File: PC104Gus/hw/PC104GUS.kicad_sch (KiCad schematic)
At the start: 40 parts, among them J1 IRQDMA_JP, J2 Conn_02x31_Top_Bottom, J3 Bus_ISA_8bit, J4 Conn_01x04_Pin, J5 SJ1-3535NG, J6 UART_TX, J7 Conn_01x02_Pin, J8 SJ1-3535NG, U1 Pico, U10 74LVC2G06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

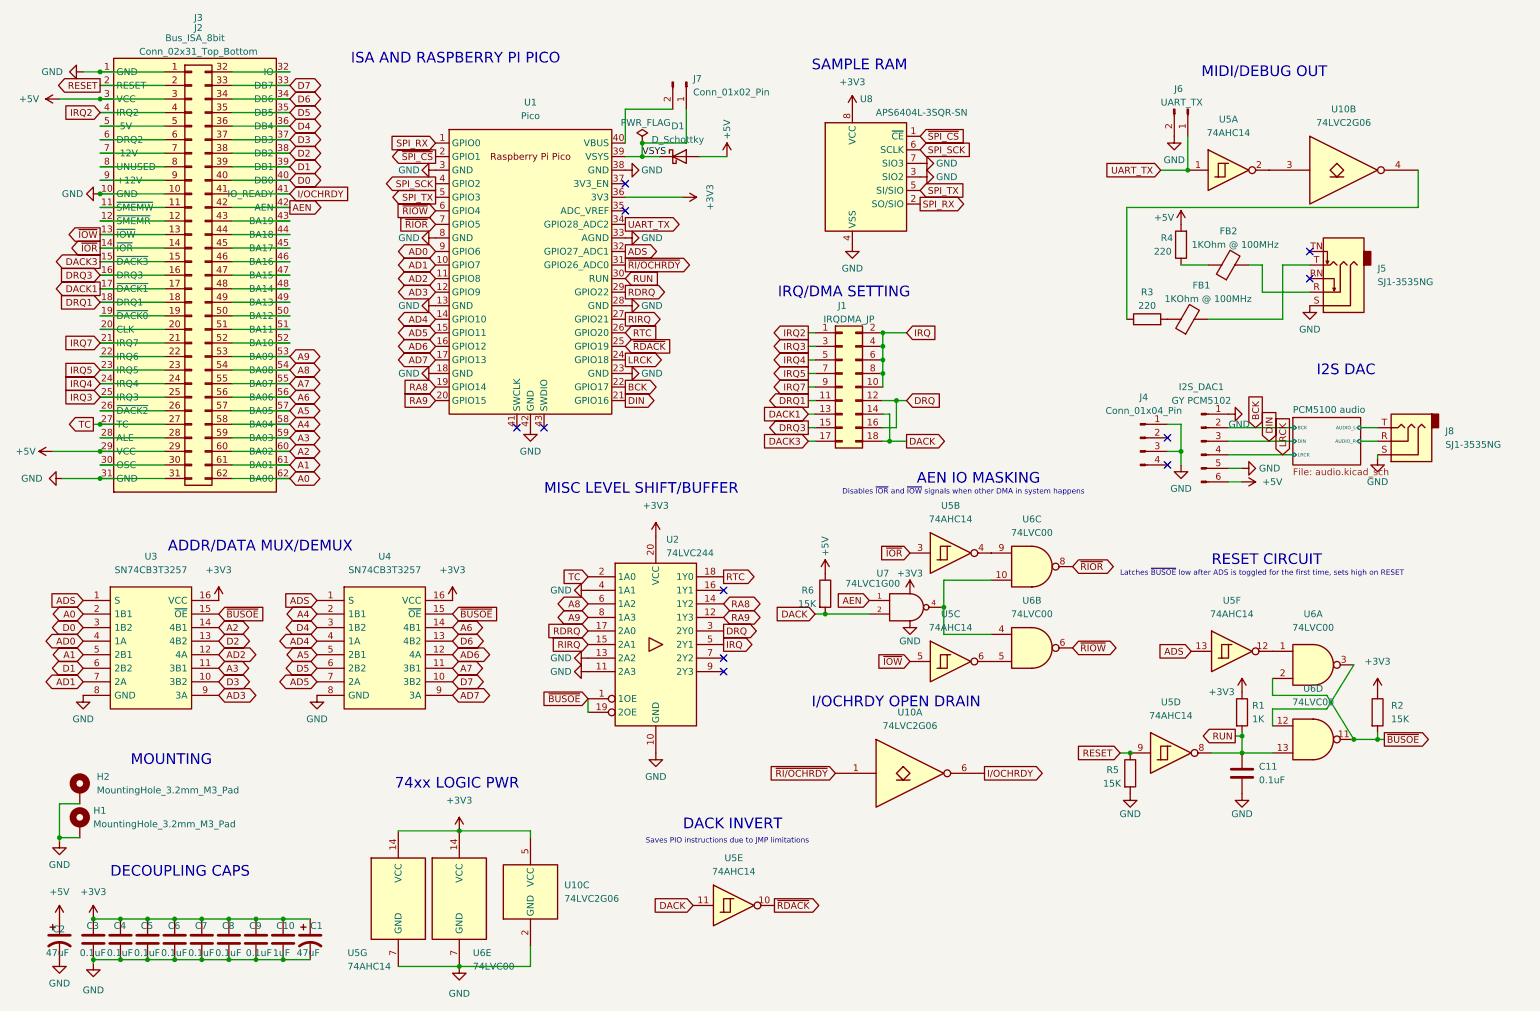
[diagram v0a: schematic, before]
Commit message: Part position complete
Added all parts, sorted part numbering and foot prints.
Beginning routing
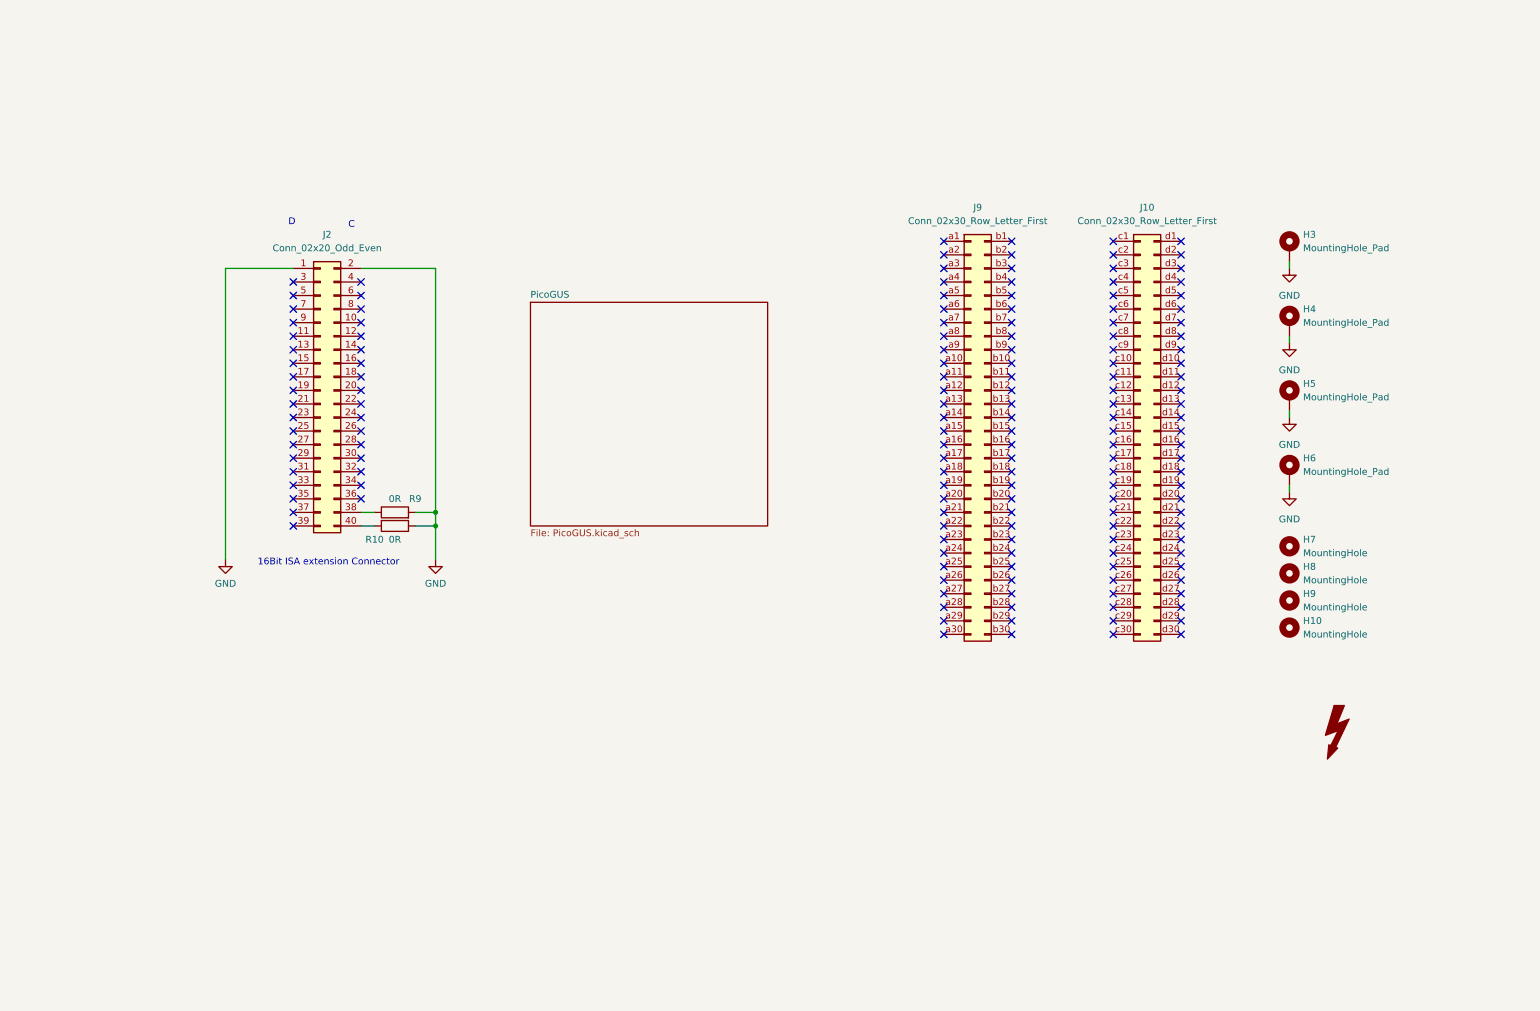
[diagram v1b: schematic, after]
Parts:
- removed C1, C2: 47uF, Capacitor_SMD:C_1206_3216Metric, symbol Device:C_Polarized_US
- removed C10: 1uF, Capacitor_SMD:C_0805_2012Metric, symbol Device:C
- removed C11, C3, C4, C5, C6, C7, C8, C9: 0.1uF, Capacitor_SMD:C_0805_2012Metric, symbol Device:C
- removed D1: D_Schottky, Diode_SMD:D_SOD-123, symbol Device:D_Schottky
- removed FB1, FB2: 1KOhm @ 100MHz, Inductor_SMD:L_0805_2012Metric, symbol Device:FerriteBead
- removed H1, H2: MountingHole_3.2mm_M3_Pad, MountingHole:MountingHole_3.2mm_M3_Pad, symbol Mechanical:MountingHole_Pad
- removed I2S_DAC1: GY PCM5102, Connector_PinHeader_2.54mm:PinHeader_1x06_P2.54mm_Vertical, symbol Connector:Conn_01x06_Pin
- removed J1: IRQDMA_JP, Connector_PinHeader_2.54mm:PinHeader_2x09_P2.54mm_Vertical, symbol Connector_Generic:Conn_02x09_Odd_Even
- removed J2: Conn_02x31_Top_Bottom, Connector_PinHeader_2.54mm:PinHeader_2x31_P2.54mm_Vertical, symbol Connector_Generic:Conn_02x31_Top_Bottom
- removed J3: Bus_ISA_8bit, PiGUS library:BUS_PC_chamfer, symbol Connector:Bus_ISA_8bit
- removed J4: Conn_01x04_Pin, Connector_PinHeader_2.54mm:PinHeader_1x04_P2.54mm_Vertical, symbol Connector:Conn_01x04_Pin
- removed J5: SJ1-3535NG, Connector_Audio:Jack_3.5mm_CUI_SJ1-3535NG_Horizontal, symbol Connector:AudioJack3_SwitchTR
- removed J6: UART_TX, Connector_PinHeader_2.54mm:PinHeader_1x02_P2.54mm_Vertical, symbol Connector:Conn_01x02_Male
- removed J7: Conn_01x02_Pin, Connector_PinHeader_2.54mm:PinHeader_1x02_P2.54mm_Vertical, symbol Connector:Conn_01x02_Pin
- removed J8: SJ1-3535NG, Connector_Audio:Jack_3.5mm_CUI_SJ1-3535NG_Horizontal, symbol Connector_Audio:AudioJack3
- removed R1: 1K, Resistor_SMD:R_0805_2012Metric, symbol Device:R
- removed R2, R5, R6: 15K, Resistor_SMD:R_0805_2012Metric, symbol Device:R
- removed R3, R4: 220, Resistor_SMD:R_0805_2012Metric, symbol Device:R
- removed U1: Pico, PiGUS library:RPi_Pico_SMD_TH, symbol PiGUS library:Pico
- removed U10: 74LVC2G06, Package_SO:TSOP-6_1.65x3.05mm_P0.95mm, symbol 74xGxx:74LVC2G06
- removed U2: 74LVC244, Package_SO:TSSOP-20_4.4x6.5mm_P0.65mm, symbol 74xx:74HC244
- removed U3, U4: SN74CB3T3257, Package_SO:TSSOP-16_4.4x5mm_P0.65mm, symbol PiGUS library:74FST3257DR2G
- removed U5: 74AHC14, Package_SO:SOIC-14_3.9x8.7mm_P1.27mm, symbol 74xx:74LS14
- removed U6: 74LVC00, Package_SO:SOIC-14_3.9x8.7mm_P1.27mm, symbol 74xx:74LS00
- removed U7: 74LVC1G00, Package_TO_SOT_SMD:SOT-23-5, symbol 74xGxx:74LVC1G00
- removed U8: APS6404L-3SQR-SN, Package_SO:SOIC-8_3.9x4.9mm_P1.27mm, symbol Memory_RAM:ESP-PSRAM32
- added FOX1: SYM_Flash_Large, PaulasKiCADFootPrint:Fox_avatar_18mm, symbol Graphic:SYM_Flash_Large
- added H10, H7, H8, H9: MountingHole, MountingHole:MountingHole_2mm, symbol Mechanical:MountingHole
- added H3, H4, H5, H6: MountingHole_Pad, MountingHole:MountingHole_3.2mm_M3_Pad_TopBottom, symbol Mechanical:MountingHole_Pad
- added J10, J9: Conn_02x30_Row_Letter_First, Connector_PinSocket_2.00mm:PinSocket_2x30_P2.00mm_Vertical, symbol Connector_Generic:Conn_02x30_Row_Letter_First
- added J2: Conn_02x20_Odd_Even, Connector_PinSocket_2.54mm:PinSocket_2x20_P2.54mm_Vertical, symbol Connector_Generic:Conn_02x20_Odd_Even
- added R10, R9: 0R, Resistor_SMD:R_0603_1608Metric, symbol Device:R
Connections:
- net GND: now also H3.1, H4.1, H5.1, H6.1, J2.1 (Pin_1), J2.2 (Pin_2), R10.1, R9.2
- new net: J2.38 (Pin_38), R9.1
- new net: J2.40 (Pin_40), R10.2
- no-connect marks 11 -> 156
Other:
- removed sheet PCM5100 audio
- added sheet PicoGUS (PicoGUS.kicad_sch)
- note added: "16Bit ISA extension Connector"
- note added: "C"
- note added: "D"
- note removed: "74xx LOGIC PWR"
- note removed: "ADDR/DATA MUX/DEMUX"
- note removed: "AEN IO MASKING"
- note removed: "DACK INVERT"
- note removed: "DECOUPLING CAPS"
- note removed: "Disables ~{IOR} and ~{IOW} signals when other DMA in system happens"
- note removed: "I/OCHRDY OPEN DRAIN"
- note removed: "I2S DAC"
- note removed: "IRQ/DMA SETTING"
- note removed: "ISA AND RASPBERRY PI PICO"
- note removed: "Latches ~{BUSOE} low after ADS is toggled for the first time, sets high on RESET"
- note removed: "MIDI/DEBUG OUT"
- note removed: "MISC LEVEL SHIFT/BUFFER"
- note removed: "MOUNTING"
- note removed: "RESET CIRCUIT"
- note removed: "SAMPLE RAM"
- note removed: "Saves PIO instructions due to JMP limitations"
- title: PicoGUS -> (none)

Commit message: PC104GUS production files
Production files generated. This build worked!
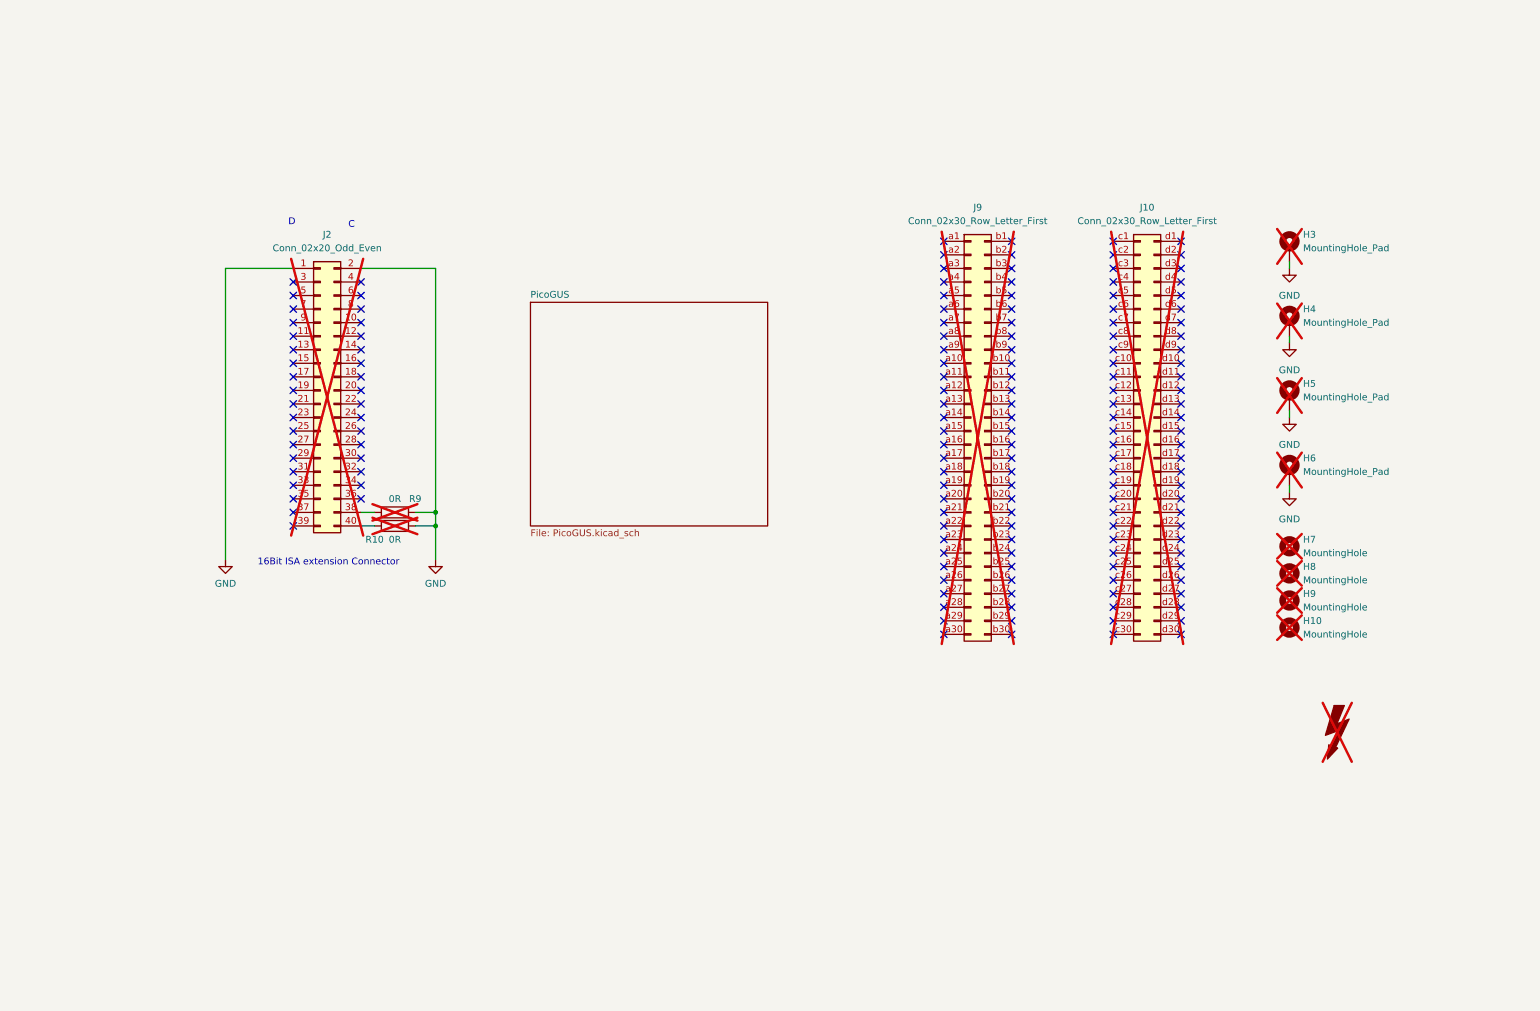
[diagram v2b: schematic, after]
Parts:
- FOX1, J10, J2, J9, R10, R9: LCSC (none) -> DNF; now not fitted
- H10, H3, H4, H5, H6, H7, H8, H9: LCSC (none) -> DNF; now not fitted; now in the parts list
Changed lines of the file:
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@@
 		(unit 1)
 		(exclude_from_sim yes)
-		(in_bom no)
-		(on_board yes)
-		(dnp no)
+		(in_bom yes)
+		(on_board yes)
+		(dnp yes)
 		(fields_autoplaced yes)
 		(property "Reference" "H9"
@@
 			)
 		)
+		(property "LCSC" "DNF"
+			(at 251.46 123.19 0)
+			(effects
+				(font
+					(size 1.27 1.27)
+				)
+				(hide yes)
+			)
+		)
 		(instances
 			(project "PC104GUS"
@@
 		(in_bom yes)
 		(on_board yes)
-		(dnp no)
+		(dnp yes)
 		(fields_autoplaced yes)
 		(property "Reference" "J9"
@@
 			)
 		)
+		(property "LCSC" "DNF"
+			(at 191.77 91.44 0)
+			(effects
+				(font
+					(size 1.27 1.27)
+				)
+				(hide yes)
+			)
+		)
 		(pin "b29"
 		)
@@
 		(unit 1)
 		(exclude_from_sim yes)
-		(in_bom no)
-		(on_board yes)
-		(dnp no)
+		(in_bom yes)
+		(on_board yes)
+		(dnp yes)
 		(fields_autoplaced yes)
 		(property "Reference" "H3"
@@
 			)
 		)
+		(property "LCSC" "DNF"
+			(at 251.46 57.15 0)
+			(effects
+				(font
+					(size 1.27 1.27)
+				)
+				(hide yes)
+			)
+		)
 		(pin "1"
 		)
@@
 		(at 260.35 147.32 0)
 		(unit 1)
-		(exclude_from_sim no)
-		(in_bom yes)
-		(on_board yes)
-		(dnp no)
+		(exclude_from_sim yes)
+		(in_bom yes)
+		(on_board yes)
+		(dnp yes)
 		(fields_autoplaced yes)
 		(property "Reference" "FOX1"
@@
 			)
 		)
-		(property "Sim.Enable" "0"
-			(at 260.35 147.32 0)
+		(property "LCSC" "DNF"
+			(at 260.35 147.32 90)
 			(effects
 				(font
@@
 		(unit 1)
 		(exclude_from_sim yes)
-		(in_bom no)
-		(on_board yes)
-		(dnp no)
+		(in_bom yes)
+		(on_board yes)
+		(dnp yes)
 		(fields_autoplaced yes)
 		(property "Reference" "H7"
@@
 		)
 		(property "Description" "Mounting Hole without connection"
+			(at 251.46 113.03 0)
+			(effects
+				(font
+					(size 1.27 1.27)
+				)
+				(hide yes)
+			)
+		)
+		(property "LCSC" "DNF"
 			(at 251.46 113.03 0)
 			(effects
@@
 		(in_bom yes)
 		(on_board yes)
-		(dnp no)
+		(dnp yes)
 		(property "Reference" "R9"
 			(at 87.63 104.14 90)
@@
 			)
 		)
+		(property "LCSC" "DNF"
+			(at 83.82 106.68 90)
+			(effects
+				(font
+					(size 1.27 1.27)
+				)
+				(hide yes)
+			)
+		)
 		(pin "2"
 		)
@@
 		(unit 1)
 		(exclude_from_sim yes)
-		(in_bom no)
-		(on_board yes)
-		(dnp no)
+		(in_bom yes)
+		(on_board yes)
+		(dnp yes)
 		(fields_autoplaced yes)
 		(property "Reference" "H4"
@@
 		)
 		(property "Description" "Mounting Hole with connection"
+			(at 251.46 71.12 0)
+			(effects
+				(font
+					(size 1.27 1.27)
+				)
+				(hide yes)
+			)
+		)
+		(property "LCSC" "DNF"
 			(at 251.46 71.12 0)
 			(effects
@@
 		(in_bom yes)
 		(on_board yes)
-		(dnp no)
+		(dnp yes)
 		(property "Reference" "R10"
 			(at 80.01 111.76 90)
@@
 			)
 		)
+		(property "LCSC" "DNF"
+			(at 83.82 109.22 90)
+			(effects
+				(font
+					(size 1.27 1.27)
+				)
+				(hide yes)
+			)
+		)
 		(pin "2"
 		)
@@
 		(unit 1)
 		(exclude_from_sim yes)
-		(in_bom no)
-		(on_board yes)
-		(dnp no)
+		(in_bom yes)
+		(on_board yes)
+		(dnp yes)
 		(fields_autoplaced yes)
 		(property "Reference" "H6"
@@
 		)
 		(property "Description" "Mounting Hole with connection"
+			(at 251.46 99.06 0)
+			(effects
+				(font
+					(size 1.27 1.27)
+				)
+				(hide yes)
+			)
+		)
+		(property "LCSC" "DNF"
 			(at 251.46 99.06 0)
 			(effects
@@
 		(unit 1)
 		(exclude_from_sim yes)
-		(in_bom no)
-		(on_board yes)
-		(dnp no)
+		(in_bom yes)
+		(on_board yes)
+		(dnp yes)
 		(fields_autoplaced yes)
 		(property "Reference" "H5"
@@
 			)
 		)
+		(property "LCSC" "DNF"
+			(at 251.46 85.09 0)
+			(effects
+				(font
+					(size 1.27 1.27)
+				)
+				(hide yes)
+			)
+		)
 		(pin "1"
 		)
@@
 		(unit 1)
 		(exclude_from_sim yes)
-		(in_bom no)
-		(on_board yes)
-		(dnp no)
+		(in_bom yes)
+		(on_board yes)
+		(dnp yes)
 		(fields_autoplaced yes)
 		(property "Reference" "H10"
@@
 			)
 		)
+		(property "LCSC" "DNF"
+			(at 251.46 128.27 0)
+			(effects
+				(font
+					(size 1.27 1.27)
+				)
+				(hide yes)
+			)
+		)
 		(instances
 			(project "PC104GUS"
@@
 		(in_bom yes)
 		(on_board yes)
-		(dnp no)
+		(dnp yes)
 		(fields_autoplaced yes)
 		(property "Reference" "J10"
@@
 			)
 		)
+		(property "LCSC" "DNF"
+			(at 223.52 91.44 0)
+			(effects
+				(font
+					(size 1.27 1.27)
+				)
+				(hide yes)
+			)
+		)
 		(pin "c28"
 		)
@@
 		(unit 1)
 		(exclude_from_sim yes)
-		(in_bom no)
-		(on_board yes)
-		(dnp no)
+		(in_bom yes)
+		(on_board yes)
+		(dnp yes)
 		(fields_autoplaced yes)
 		(property "Reference" "H8"
@@
 			)
 		)
+		(property "LCSC" "DNF"
+			(at 251.46 118.11 0)
+			(effects
+				(font
+					(size 1.27 1.27)
+				)
+				(hide yes)
+			)
+		)
 		(instances
 			(project "PC104GUS"
@@
 		(in_bom yes)
 		(on_board yes)
-		(dnp no)
+		(dnp yes)
 		(fields_autoplaced yes)
 		(property "Reference" "J2"
@@
 			(at 69.85 83.82 0)
 			(effects
+				(font
+					(size 1.27 1.27)
+				)
+				(hide yes)
+			)
+		)
+		(property "LCSC" "DNF"
+			(at 69.85 83.82 0)
+			(effects
